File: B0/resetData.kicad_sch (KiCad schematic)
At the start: 2 parts, among them U014 74HCT08, U021 74HCT08

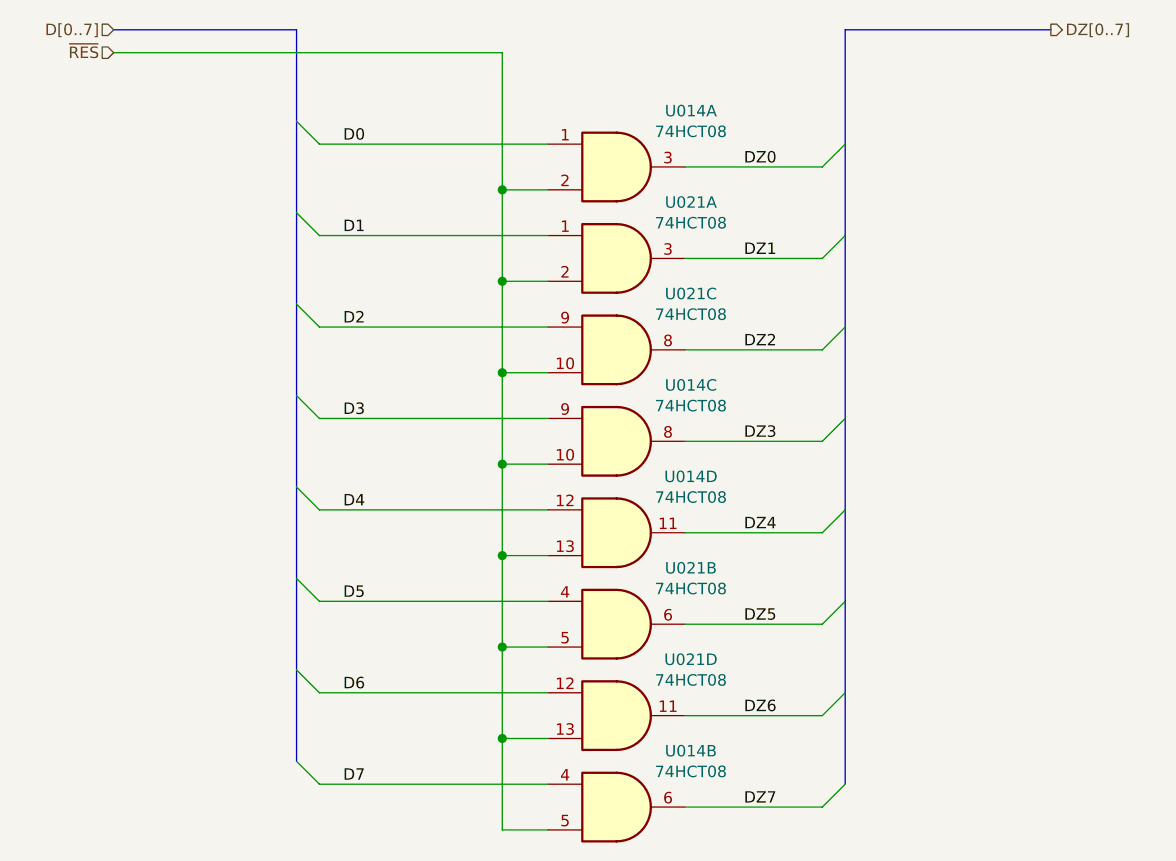
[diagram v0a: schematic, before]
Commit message: B1 CREGA added
Work started on b1. CREGA added.
Minor changes to B0 schematic properties.
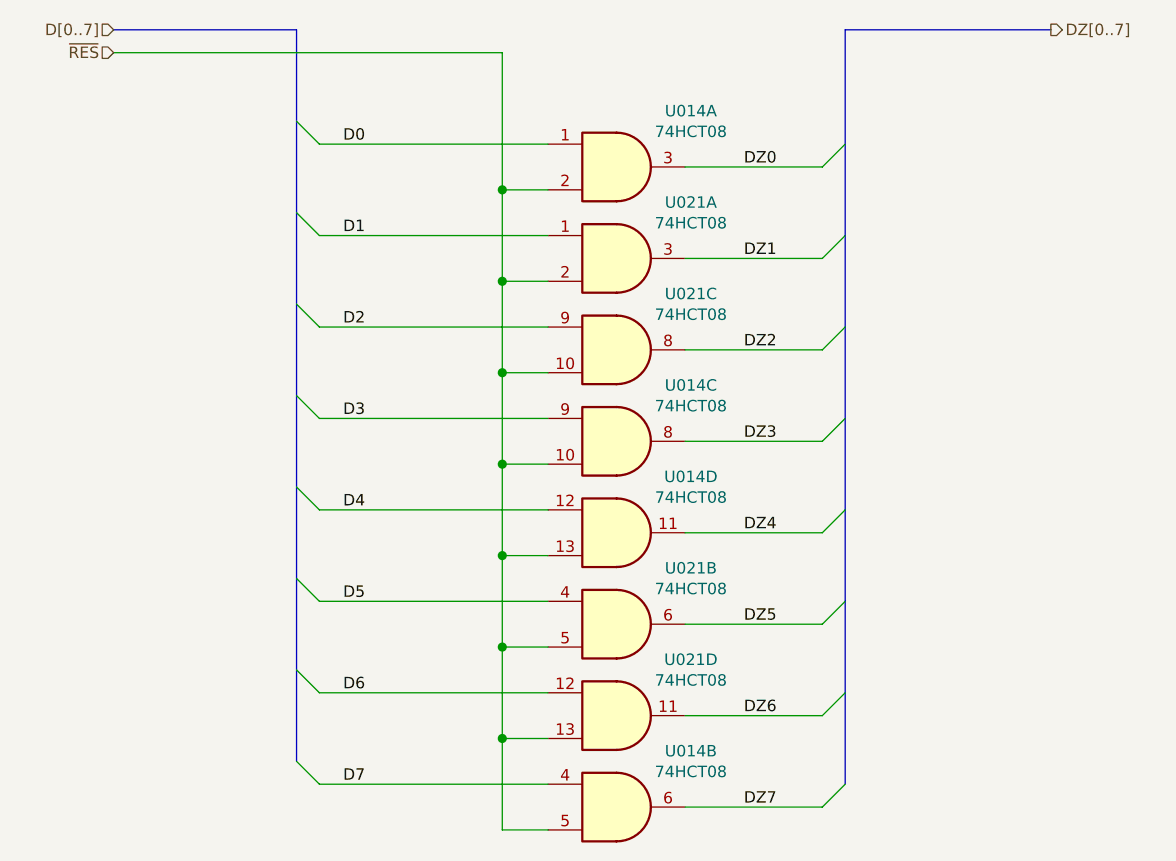
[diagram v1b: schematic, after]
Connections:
- net ~RES renamed ~{RES}
